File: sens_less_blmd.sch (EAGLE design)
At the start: 7 parts

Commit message: インバータ部を設計した
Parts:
- added C1, C2, C3, C4, C5, C6: 4.7n, rcl:C-EUC1608
- added C7, C8, C9: 0.1u, rcl:C-EUC1608
- added CPOL1, CPOL2, CPOL3: 330u, user_rcl:C_DEKAI
- added R1, R2, R3, R4, R5, R6: 10, user_rcl:R_REG
- added R10, R11, R12, R7, R8, R9: 10k, user_rcl:R_REG
- added U$10, U$11, U$12, U$13, U$8, U$9: SBR10M100P5Q, user_diode:SBR10M100P5Q
- added U$14, U$15, U$16: ACS711, user_ic:ACS711
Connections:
- new net GHA: R1.1, U$1.PIN11_GHA
- new net GHB: R3.1, U$1.PIN7_GHB
- new net GHC: R5.1, U$1.PIN3_GHC
- new net GLA: R2.1, U$1.PIN10_GLA
- new net GLB: R4.1, U$1.PIN6_GLB
- new net GLC: R6.1, U$1.PIN2_GLC
- new net GNDA: U$1.PAD
- new net MCU_GND: U$14.5_GND, U$15.5_GND, U$16.5_GND
- new net MCU_VCC: U$14.8_VCC, U$15.8_VCC, U$16.8_VCC
- new net N$1: C1.1, R1.2, R7.2, U$2.PIN1_G
- new net N$10: C2.2, R12.1, U$14.1_IP+, U$14.2_IP+, U$3.PIN3_S, U$9.A1, U$9.A2
- new net N$12: U$14.3_IP-, U$14.4_IP-, U$15.3_IP-, U$15.4_IP-, U$16.3_IP-, U$16.4_IP-
- new net N$13: C5.2, R11.1, U$13.A1, U$13.A2, U$16.1_IP+, U$16.2_IP+, U$7.PIN3_S
- new net N$15: C4.2, R10.1, U$10.A1, U$10.A2, U$15.1_IP+, U$15.2_IP+, U$5.PIN3_S
- new net N$16: U$15.6_FAULT
- new net N$2: C2.1, R12.2, R2.2, U$3.PIN1_G
- new net N$20: U$16.6_FAULT
- new net N$3: C4.1, R10.2, R4.2, U$5.PIN1_G
- new net N$4: C3.1, R3.2, R9.2, U$4.PIN1_G
- new net N$5: C6.1, R5.2, R8.2, U$6.PIN1_G
- new net N$6: C5.1, R11.2, R6.2, U$7.PIN1_G
- new net N$9: U$14.6_FAULT
- new net PHASE_U: C1.2, R7.1, U$2.PIN3_S, U$3.PIN2_D, U$8.A1, U$8.A2, U$9.K
- new net PHASE_U_I: U$14.7_VIOUT
- new net PHASE_V: C3.2, R9.1, U$10.K, U$11.A1, U$11.A2, U$4.PIN3_S, U$5.PIN2_D
- new net PHASE_V_I: U$15.7_VIOUT
- new net PHASE_W: C6.2, R8.1, U$12.A1, U$12.A2, U$13.K, U$6.PIN3_S, U$7.PIN2_D
- new net PHASE_W_I: U$16.7_VIOUT
- new net VCC: C7.1, C8.1, C9.1, CPOL1.+, CPOL2.+, CPOL3.+, U$11.K, U$12.K, U$2.PIN2_D, U$4.PIN2_D, U$6.PIN2_D, U$8.K
- net GND: now also C7.2, C8.2, C9.2, CPOL1.-, CPOL2.-, CPOL3.-, U$1.PIN1_LSS; no longer U$1.PAD

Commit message: ドライバ側回路図の完成
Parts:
- added C10: 1u, rcl:C-EUC1608
- added C11, C12, C13: 0.22u, rcl:C-EUC1608
- added C14: 10u, rcl:C-EUC1608
- added C15, C17, C18, C19, C20, C21, C22: 0.1u, rcl:C-EUC1608
- added C16: (no value), rcl:C-EUC1608
- added JP1, JP2, JP3: (no value), pinhead:PINHD-1X4
- added JP4, JP5: (no value), pinhead:PINHD-1X8
- added LED1: (no value), user_leds:1608LED
- added R13, R14, R15, R18, R20: 10k, user_rcl:R_REG
- added R16, R17: (no value), user_rcl:R_REG
- added R19: 470, user_rcl:R_REG
- added R21: 0, user_rcl:R_REG
- added R_I1, R_I2: 10k, user_rcl:R_SHUGOU2
- added R_I3, R_I4: 10k, user_rcl:R_SHUGOU
- added U$17: SOT23_NFET, user_tr_fet_igbt:SOT23_NFET
- added U$18: TLP291, user_ic:TLP291
- added U$19, U$20, U$21: TLP2105, user_ic:TLP2105
- added U$22: XT60, user_conector:XT60
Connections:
- new net AHI: R_I2.4, U$1.PIN23_AHI, U$21.PIN6_VO2
- new net AHI_IN: JP5.3, R_I4.4
- new net ALO: R_I2.1, U$1.PIN24_ALO, U$21.PIN7_VO1
- new net ALO_IN: JP5.1, R_I4.1
- new net BHI: R_I1.4, U$1.PIN25_BHI, U$20.PIN6_VO2
- new net BHI_IN: JP4.7, R_I3.4
- new net BLO: R_I1.3, U$1.PIN26_BLO, U$20.PIN7_VO1
- new net BLO_IN: JP4.5, R_I3.3
- new net CHI: R_I1.2, U$1.PIN27_CHI, U$19.PIN6_VO2
- new net CHI_IN: JP4.3, R_I3.2
- new net CLO: R_I1.1, U$1.PIN28_CLO, U$19.PIN7_VO1
- new net CLO_IN: JP4.1, R_I3.1
- new net FAULT: R18.1, U$1.PIN22_FAULT, U$17.PIN1_G
- new net FAULT_O: JP5.5, R20.1, U$18.PIN4_TR_C
- new net N$11: LED1.K, U$17.PIN2_D, U$18.PIN2_KSODE
- new net N$14: LED1.A, R19.1, U$18.PIN1_ANODE
- new net N$17: C12.2, U$1.PIN9_CB
- new net N$18: C11.2, U$1.PIN5_CC
- new net N$19: R_I4.8, U$21.PIN1_ANODE1
- new net N$21: C19.1, C9.1, CPOL3.+, U$12.K, U$6.PIN2_D
- new net N$22: R_I3.5, U$20.PIN4_ANODE2
- new net N$23: R_I3.6, U$20.PIN1_ANODE1
- new net N$24: R_I3.7, U$19.PIN4_ANODE2
- new net N$25: R_I3.8, U$19.PIN1_ANODE1
- new net N$7: C10.1, U$1.PIN16_CP1
- new net N$8: C10.2, U$1.PIN15_CP2
- new net PHASE_U_FAULT: JP1.3, R13.1, U$14.6_FAULT
- new net PHASE_V_FAULT: JP2.3, R14.1, U$15.6_FAULT
- new net PHASE_W_FAULT: JP3.3, R15.1, U$16.6_FAULT
- new net V5: C16.1, C20.1, C21.1, C22.1, R16.2, R18.2, R19.2, R_I1.5, R_I1.6, R_I1.7, R_I1.8, R_I2.5, R_I2.8, U$1.PIN20_V3,V5,VDDM, U$19.PIN8_VCC, U$20.PIN8_VCC, U$21.PIN8_VCC
- new net VDSTH: R16.1, R17.2, U$1.PIN21_VDSTH
- net GND: now also C17.2, C19.2, R21.2, U$14.3_IP-, U$14.4_IP-, U$16.3_IP-, U$16.4_IP-, U$22.-; no longer C8.2, CPOL2.-
- net GNDA: now also C14.2, C15.2, C16.2, C20.2, C21.2, C22.2, R17.1, R21.1, U$1.PIN19_GND, U$17.PIN3_S, U$19.PIN5_GND, U$20.PIN5_GND, U$21.PIN5_GND
- net MCU_GND: now also JP1.4, JP2.4, JP3.4, JP4.2, JP4.4, JP4.6, JP4.8, JP5.2, JP5.4, JP5.6, U$18.PIN3_TR_E, U$19.PIN2_KSODE1, U$19.PIN3_KSODE2, U$20.PIN2_KSODE1, U$20.PIN3_KSODE2, U$21.PIN2_KSODE1, U$21.PIN3_KSODE2
- net MCU_VCC: now also JP1.1, JP2.1, JP3.1, JP5.7, JP5.8, R13.2, R14.2, R15.2, R20.2
- net N$12: now also C18.2, C8.2, CPOL2.-; no longer U$14.3_IP-, U$14.4_IP-, U$16.3_IP-, U$16.4_IP-
- net N$16: now also C13.2, U$1.PIN13_CA; no longer U$15.6_FAULT
- net N$20: now also R_I4.5, U$21.PIN4_ANODE2; no longer U$16.6_FAULT
- net N$9: now also C14.1, U$1.PIN14_VREG; no longer U$14.6_FAULT
- net PHASE_U: now also C13.1, U$1.PIN12_SA
- net PHASE_U_I: now also JP1.2
- net PHASE_V: now also C12.1, U$1.PIN8_SB
- net PHASE_V_I: now also JP2.2
- net PHASE_W: now also C11.1, U$1.PIN4_SC
- net PHASE_W_I: now also JP3.2
- net VCC: now also C15.1, C17.1, C18.1, U$1.PIN17_VBB, U$1.PIN18_VBRG, U$22.+; no longer C9.1, CPOL3.+, U$12.K, U$6.PIN2_D
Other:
- moved on the sheet: C1, C2, C3, C4, C5, C6, C7, C8, C9, CPOL1, CPOL2, CPOL3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

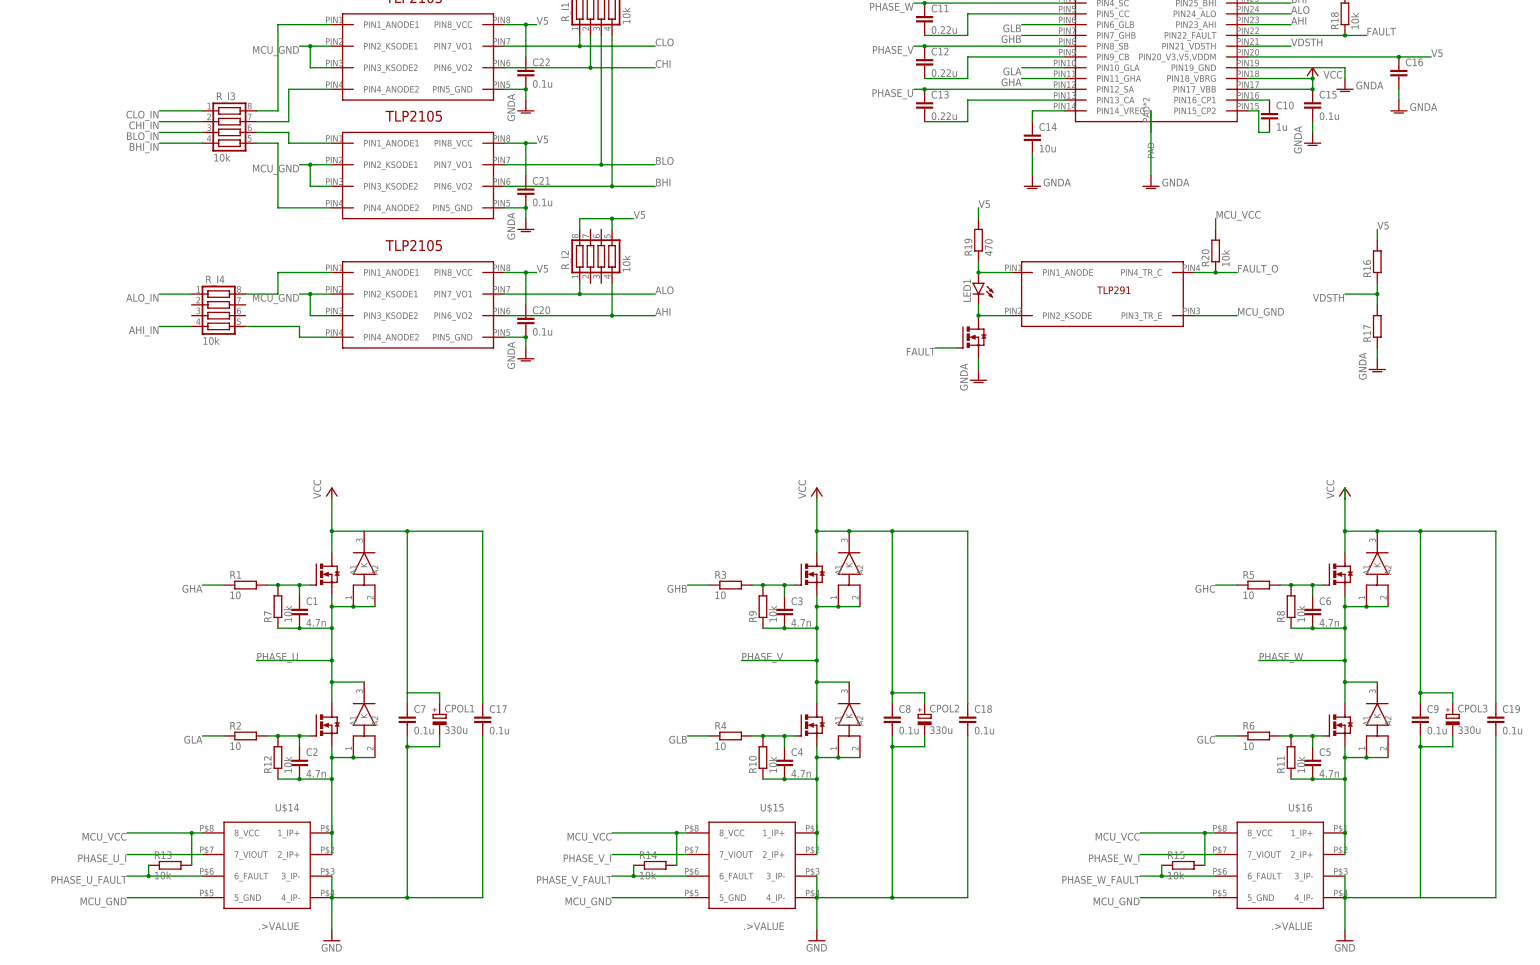
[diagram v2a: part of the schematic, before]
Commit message: 電流センサの測定位置を変えた
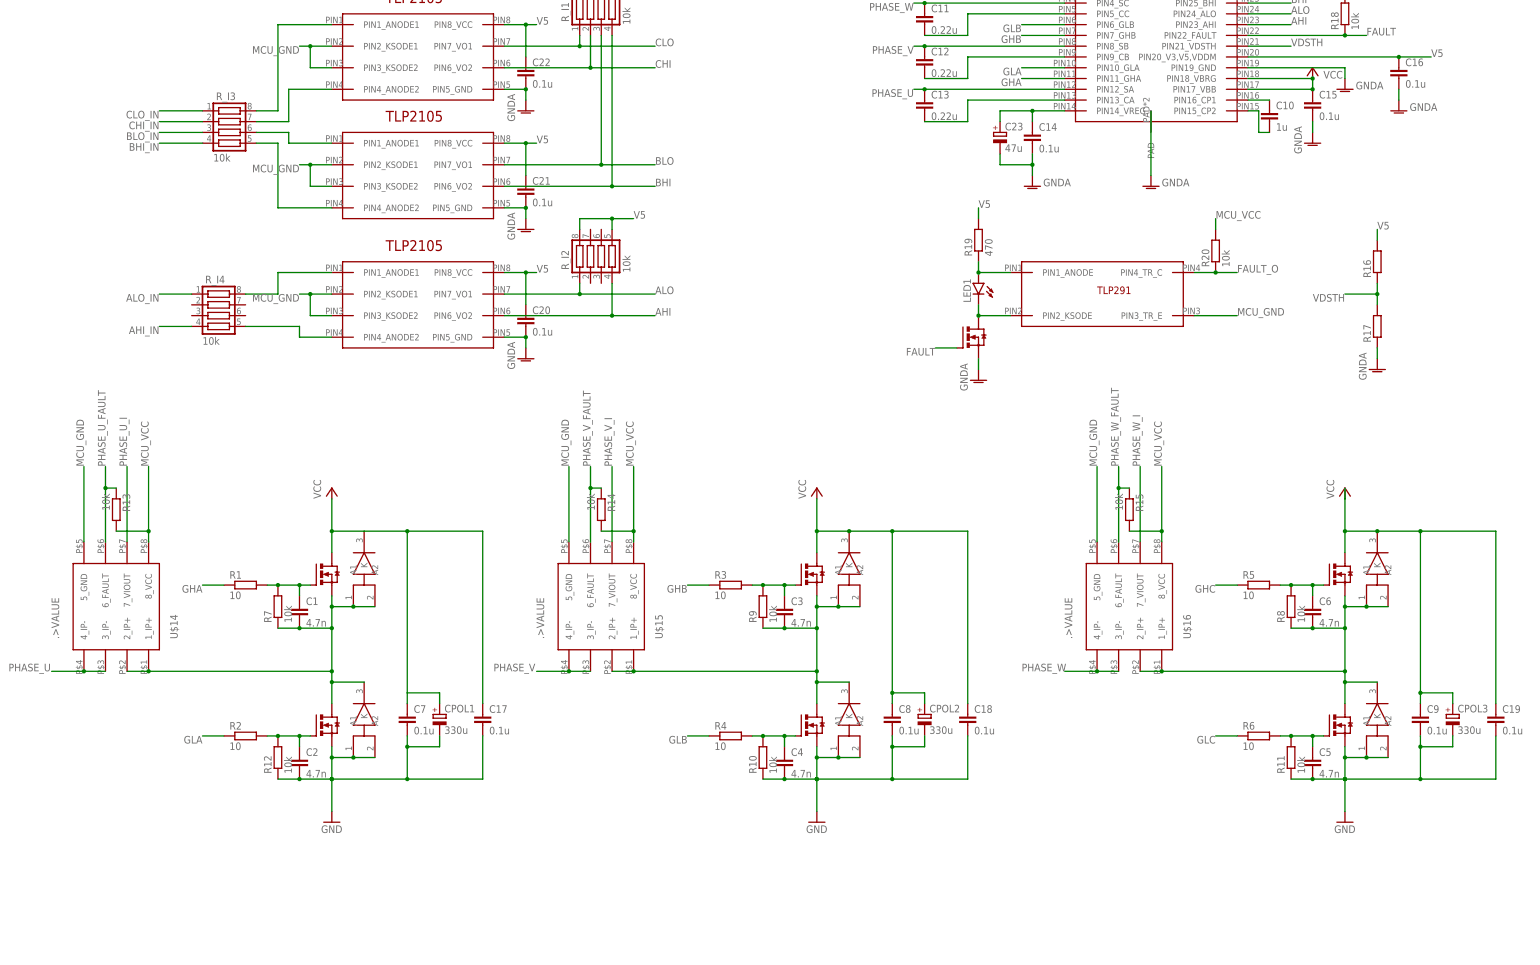
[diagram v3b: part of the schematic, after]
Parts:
- added C23: 47u, rcl:CPOL-EU153CLV-0605
- C14: value 10u -> 0.1u
- C16: value (none) -> 0.1u
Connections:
- removed net N$13: C5.2, R11.1, U$13.A1, U$13.A2, U$16.1_IP+, U$16.2_IP+, U$7.PIN3_S
- removed net N$15: C4.2, R10.1, U$10.A1, U$10.A2, U$15.1_IP+, U$15.2_IP+, U$5.PIN3_S
- new net N$26: C1.2, R7.1, U$14.1_IP+, U$14.2_IP+, U$2.PIN3_S, U$3.PIN2_D, U$8.A1, U$8.A2, U$9.K
- net GND: now also C18.2, C2.2, C4.2, C5.2, C8.2, CPOL2.-, R10.1, R11.1, R12.1, U$10.A1, U$10.A2, U$13.A1, U$13.A2, U$3.PIN3_S, U$5.PIN3_S, U$7.PIN3_S, U$9.A1, U$9.A2; no longer U$14.3_IP-, U$14.4_IP-, U$16.3_IP-, U$16.4_IP-
- net GNDA: now also C23.-
- net N$10: now also C6.2, R8.1, U$12.A1, U$12.A2, U$13.K, U$16.1_IP+, U$16.2_IP+, U$6.PIN3_S, U$7.PIN2_D; no longer C2.2, R12.1, U$14.1_IP+, U$14.2_IP+, U$3.PIN3_S, U$9.A1, U$9.A2
- net N$12: now also C3.2, R9.1, U$10.K, U$11.A1, U$11.A2, U$15.1_IP+, U$15.2_IP+, U$4.PIN3_S, U$5.PIN2_D; no longer C18.2, C8.2, CPOL2.-, U$15.3_IP-, U$15.4_IP-
- net N$9: now also C23.+
- net PHASE_U: now also U$14.3_IP-, U$14.4_IP-; no longer C1.2, R7.1, U$2.PIN3_S, U$3.PIN2_D, U$8.A1, U$8.A2, U$9.K
- net PHASE_V: now also U$15.3_IP-, U$15.4_IP-; no longer C3.2, R9.1, U$10.K, U$11.A1, U$11.A2, U$4.PIN3_S, U$5.PIN2_D
- net PHASE_W: now also U$16.3_IP-, U$16.4_IP-; no longer C6.2, R8.1, U$12.A1, U$12.A2, U$13.K, U$6.PIN3_S, U$7.PIN2_D
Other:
- moved on the sheet: R13, R14, R15, U$14, U$15, U$16

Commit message: 配置を大まかにきめた
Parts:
- removed C17, C18, C19, C20, C21, C22, C8, C9: 0.1u, rcl:C-EUC1608
- removed CPOL3: 330u, user_rcl:C_DEKAI
- removed JP1, JP2, JP3: (no value), pinhead:PINHD-1X4
- removed JP4, JP5: (no value), pinhead:PINHD-1X8
- removed R14, R15, R20: 10k, user_rcl:R_REG
- removed R19: 470, user_rcl:R_REG
- removed U$16: ACS711, user_ic:ACS711
- removed U$17: SOT23_NFET, user_tr_fet_igbt:SOT23_NFET
- removed U$18: TLP291, user_ic:TLP291
- removed U$19, U$20, U$21: TLP2105, user_ic:TLP2105
- removed U$6, U$7: IPD034N06N3G, user_tr_fet_igbt:IPD034N06N3G
- added CON1: (no value), user_conector:XH_3P
- added CON2, CON3: (no value), user_conector:XH_4P
- added CON4: (no value), user_conector:XH_8P
- added IC_1: (no value), user_ic:TLP291
- added LED2: (no value), user_leds:1608LED
- added R_I5: (no value), user_rcl:R_SHUGOU
- added TR1, TR2, TR3, TR4, TR5, TR6: (no value), user_tr_fet_igbt:SKI03021
- C1, C2, C3, C4: value 4.7n -> 0.1u
- C5, C6: value 4.7n -> (none)
- R13, R_I4: value 10k -> (none)
- R_I1: value 10k -> (none); device user_rcl:R_SHUGOU2 -> user_rcl:R_SHUGOU
- R_I3: device user_rcl:R_SHUGOU -> user_rcl:R_SHUGOU2
- U$2, U$3, U$4: value IPD034N06N3G -> TLP2105; device user_tr_fet_igbt:IPD034N06N3G -> user_ic:TLP2105
- U$5: value IPD034N06N3G -> FDC6305; device user_tr_fet_igbt:IPD034N06N3G -> user_tr_fet_igbt:FDC6305
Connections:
- removed net AHI_IN: JP5.3, R_I4.4
- removed net ALO_IN: JP5.1, R_I4.1
- removed net BHI_IN: JP4.7, R_I3.4
- removed net BLO_IN: JP4.5, R_I3.3
- removed net CHI_IN: JP4.3, R_I3.2
- removed net CLO_IN: JP4.1, R_I3.1
- removed net MCU_GND: JP1.4, JP2.4, JP3.4, JP4.2, JP4.4, JP4.6, JP4.8, JP5.2, JP5.4, JP5.6, U$14.5_GND, U$15.5_GND, U$16.5_GND, U$18.PIN3_TR_E, U$19.PIN2_KSODE1, U$19.PIN3_KSODE2, U$20.PIN2_KSODE1, U$20.PIN3_KSODE2, U$21.PIN2_KSODE1, U$21.PIN3_KSODE2
- removed net MCU_VCC: JP1.1, JP2.1, JP3.1, JP5.7, JP5.8, R13.2, R14.2, R15.2, R20.2, U$14.8_VCC, U$15.8_VCC, U$16.8_VCC
- removed net N$10: C6.2, R8.1, U$12.A1, U$12.A2, U$13.K, U$16.1_IP+, U$16.2_IP+, U$6.PIN3_S, U$7.PIN2_D
- removed net N$11: LED1.K, U$17.PIN2_D, U$18.PIN2_KSODE
- removed net N$12: C3.2, R9.1, U$10.K, U$11.A1, U$11.A2, U$15.1_IP+, U$15.2_IP+, U$4.PIN3_S, U$5.PIN2_D
- removed net N$14: LED1.A, R19.1, U$18.PIN1_ANODE
- removed net N$26: C1.2, R7.1, U$14.1_IP+, U$14.2_IP+, U$2.PIN3_S, U$3.PIN2_D, U$8.A1, U$8.A2, U$9.K
- removed net PHASE_U_FAULT: JP1.3, R13.1, U$14.6_FAULT
- removed net PHASE_U_I: JP1.2, U$14.7_VIOUT
- removed net PHASE_V_FAULT: JP2.3, R14.1, U$15.6_FAULT
- removed net PHASE_V_I: JP2.2, U$15.7_VIOUT
- removed net PHASE_W_FAULT: JP3.3, R15.1, U$16.6_FAULT
- removed net PHASE_W_I: JP3.2, U$16.7_VIOUT
- new net AGND: LED2.K, U$5.PIN2_S2, U$5.PIN5_S1
- new net CURRENT_U: U$14.1_IP+, U$14.2_IP+
- new net CURRENT_W: U$15.1_IP+, U$15.2_IP+
- new net GNDIO: IC_1.3_E, U$2.PIN2_KSODE1, U$2.PIN3_KSODE2, U$3.PIN2_KSODE1, U$3.PIN3_KSODE2, U$4.PIN2_KSODE1, U$4.PIN3_KSODE2
- new net IAHI: R_I5.2
- new net IALO: R_I5.1
- new net IBHI: R_I4.4
- new net IBLO: R_I4.3
- new net ICHI: R_I4.2
- new net ICLO: R_I4.1
- new net N$27: R_I4.6, U$3.PIN1_ANODE1
- new net N$28: R_I4.5, U$3.PIN4_ANODE2
- new net N$29: R_I5.8, U$4.PIN1_ANODE1
- new net N$30: R_I5.7, U$4.PIN4_ANODE2
- new net N$31: CON1.PIN3
- new net N$32: CON1.PIN2
- new net N$33: CON1.PIN1
- new net N$34: CON2.PIN4
- new net N$35: CON2.PIN3
- new net N$36: CON2.PIN2
- new net N$37: CON2.PIN1
- new net N$38: CON3.PIN4
- new net N$39: CON3.PIN3
- new net N$40: CON3.PIN2
- new net N$41: CON3.PIN1
- new net N$42: CON4.PIN8
- new net N$43: CON4.PIN7
- new net N$44: CON4.PIN6
- new net N$45: CON4.PIN5
- new net N$46: CON4.PIN4
- new net N$47: CON4.PIN3
- new net N$48: CON4.PIN2
- new net N$49: CON4.PIN1
- new net U_GND: C5.2, U$14.5_GND
- new net U_OUT: U$14.7_VIOUT
- new net U_VCC: C5.1, U$14.8_VCC
- new net VCCIO: R13.2
- new net W_GND: C6.2, U$15.5_GND
- new net W_OUT: U$15.7_VIOUT
- new net W_VCC: C6.1, U$15.8_VCC
- net AHI: now also R_I2.8, U$4.PIN6_VO2; no longer R_I2.4, U$21.PIN6_VO2
- net ALO: now also R_I2.7, U$4.PIN7_VO1; no longer R_I2.1, U$21.PIN7_VO1
- net BHI: now also R_I2.6, U$3.PIN6_VO2; no longer R_I1.4, U$20.PIN6_VO2
- net BLO: now also R_I2.5, U$3.PIN7_VO1; no longer R_I1.3, U$20.PIN7_VO1
- net CHI: now also R_I3.8, U$2.PIN6_VO2; no longer R_I1.2, U$19.PIN6_VO2
- net CLO: now also R_I3.7, U$2.PIN7_VO1; no longer R_I1.1, U$19.PIN7_VO1
- net FAULT: now also U$5.PIN1_G1, U$5.PIN3_G2; no longer U$17.PIN1_G
- net FAULT_O: now also IC_1.4_C, R13.1; no longer JP5.5, R20.1, U$18.PIN4_TR_C
- net GND: now also C1.2, TR1.PIN3_S, TR4.PIN3_S, TR6.PIN3_S; no longer C17.2, C18.2, C19.2, C2.2, C4.2, C5.2, C8.2, C9.2, CPOL3.-, U$3.PIN3_S, U$5.PIN3_S, U$7.PIN3_S
- net GNDA: now also C2.2, C3.2, C4.2, R_I2.1, R_I2.2, R_I2.3, R_I2.4, R_I3.1, R_I3.2, U$2.PIN5_GND, U$3.PIN5_GND, U$4.PIN5_GND; no longer C20.2, C21.2, C22.2, U$17.PIN3_S, U$19.PIN5_GND, U$20.PIN5_GND, U$21.PIN5_GND
- net N$1: now also TR2.PIN1_G; no longer C1.1, U$2.PIN1_G
- net N$19: now also LED1.K, U$5.PIN4_D2; no longer R_I4.8, U$21.PIN1_ANODE1
- net N$2: now also TR1.PIN1_G; no longer C2.1, U$3.PIN1_G
- net N$20: now also IC_1.2_K, U$5.PIN6_D1; no longer R_I4.5, U$21.PIN4_ANODE2
- net N$21: now also IC_1.1_A, R_I1.4; no longer C19.1, C9.1, CPOL3.+, U$12.K, U$6.PIN2_D
- net N$22: now also LED1.A, R_I1.3; no longer R_I3.5, U$20.PIN4_ANODE2
- net N$23: now also LED2.A, R_I1.1; no longer R_I3.6, U$20.PIN1_ANODE1
- net N$24: now also R_I4.8, U$2.PIN1_ANODE1; no longer R_I3.7, U$19.PIN4_ANODE2
- net N$25: now also R_I4.7, U$2.PIN4_ANODE2; no longer R_I3.8, U$19.PIN1_ANODE1
- net N$3: now also TR4.PIN1_G; no longer C4.1, U$5.PIN1_G
- net N$4: now also TR3.PIN1_G; no longer C3.1, U$4.PIN1_G
- net N$5: now also TR5.PIN1_G; no longer C6.1, U$6.PIN1_G
- net N$6: now also TR6.PIN1_G; no longer C5.1, U$7.PIN1_G
- net PHASE_U: now also R7.1, TR1.PIN2_D, TR2.PIN3_S, U$8.A1, U$8.A2, U$9.K
- net PHASE_V: now also R9.1, TR3.PIN3_S, TR4.PIN2_D, U$10.K, U$11.A1, U$11.A2; no longer U$15.3_IP-, U$15.4_IP-
- net PHASE_W: now also R8.1, TR5.PIN3_S, TR6.PIN2_D, U$12.A1, U$12.A2, U$13.K, U$15.3_IP-, U$15.4_IP-; no longer U$16.3_IP-, U$16.4_IP-
- net V5: now also C2.1, C3.1, C4.1, U$2.PIN8_VCC, U$3.PIN8_VCC, U$4.PIN8_VCC; no longer C20.1, C21.1, C22.1, R19.2, R_I1.7, R_I2.5, R_I2.8, U$19.PIN8_VCC, U$20.PIN8_VCC, U$21.PIN8_VCC
- net VCC: now also C1.1, TR2.PIN2_D, TR3.PIN2_D, TR5.PIN2_D, U$12.K; no longer C17.1, C18.1, C8.1, U$2.PIN2_D, U$4.PIN2_D
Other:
- moved on the sheet: C1, C10, C11, C12, C13, C14, C15, C16, C2, C23, C3, C4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

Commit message: 配置を少し整えた
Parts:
- R13: value (none) -> 10k
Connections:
- removed net N$31: CON1.PIN3
- removed net N$32: CON1.PIN2
- removed net N$33: CON1.PIN1
- removed net N$34: CON2.PIN4
- removed net N$36: CON2.PIN2
- removed net N$37: CON2.PIN1
- removed net N$38: CON3.PIN4
- removed net N$40: CON3.PIN2
- removed net N$41: CON3.PIN1
- removed net N$42: CON4.PIN8
- removed net N$43: CON4.PIN7
- removed net N$44: CON4.PIN6
- removed net N$45: CON4.PIN5
- removed net N$46: CON4.PIN4
- removed net N$47: CON4.PIN3
- removed net N$48: CON4.PIN2
- removed net N$49: CON4.PIN1
- net FAULT_O: now also CON1.PIN2
- net GNDIO: now also CON1.PIN1, CON4.PIN1
- net IAHI: now also CON4.PIN3
- net IALO: now also CON4.PIN4
- net IBHI: now also CON4.PIN5
- net IBLO: now also CON4.PIN6
- net ICHI: now also CON4.PIN7
- net ICLO: now also CON4.PIN8
- net U_GND: now also CON2.PIN1
- net U_OUT: now also CON2.PIN2
- net U_VCC: now also CON2.PIN4
- net VCCIO: now also CON1.PIN3
- net W_GND: now also CON3.PIN1
- net W_OUT: now also CON3.PIN2
- net W_VCC: now also CON3.PIN4
